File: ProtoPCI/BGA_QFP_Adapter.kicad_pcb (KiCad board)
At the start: 2 copper layers, 31 x 31 mm, 2 parts

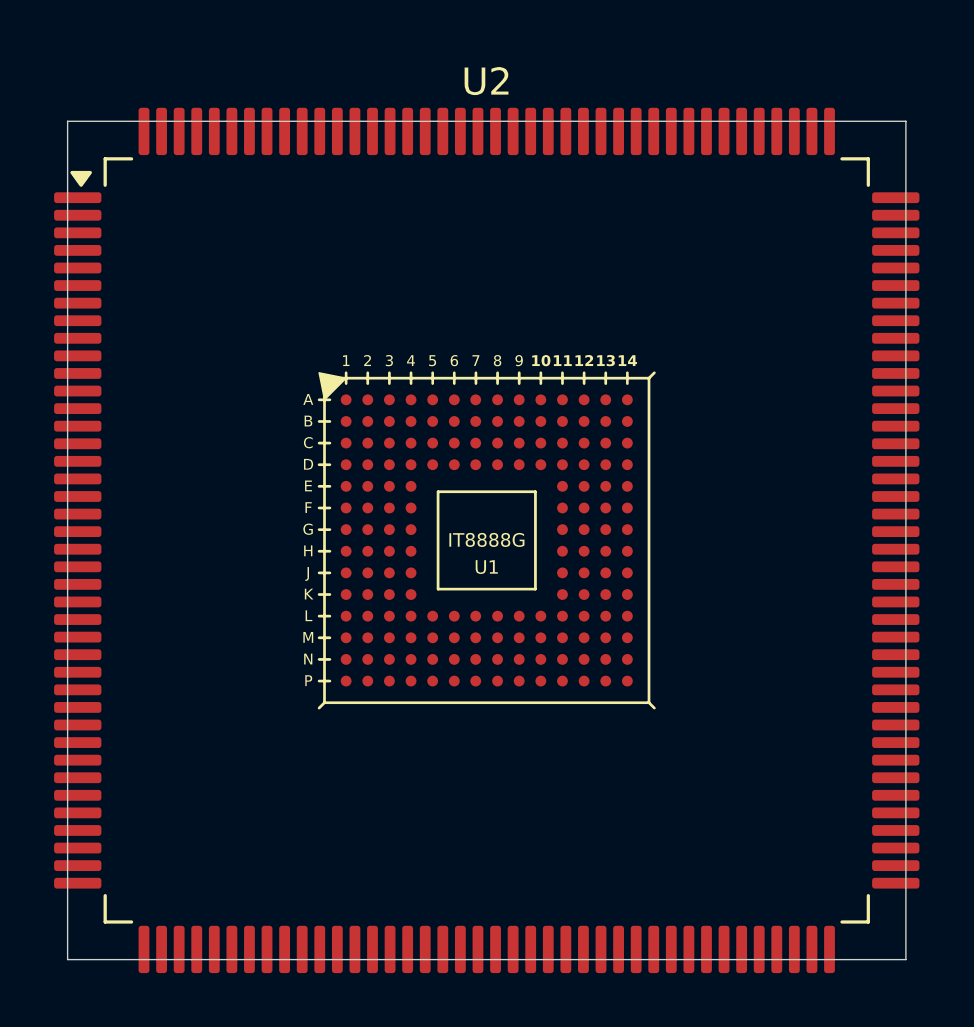
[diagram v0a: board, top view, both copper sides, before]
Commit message: Initial BGA to QFP Adapter for QFP replacement via BGA
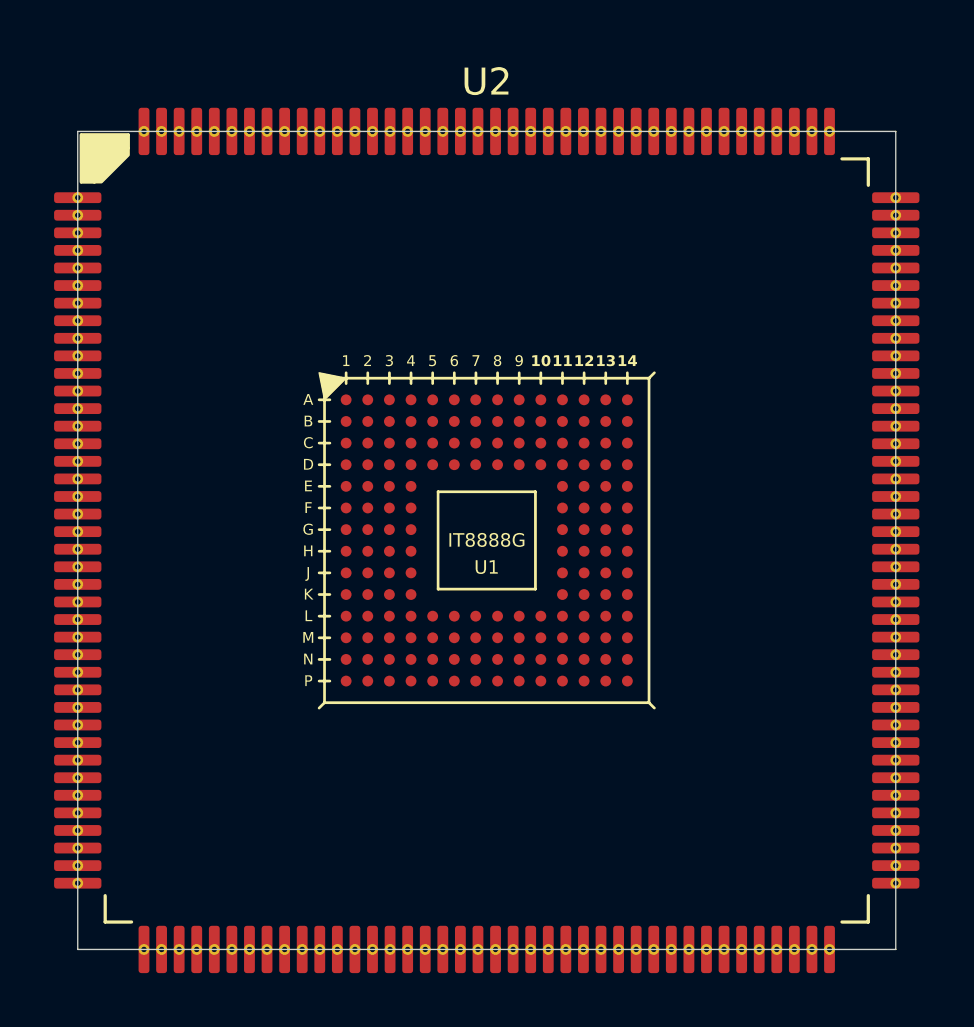
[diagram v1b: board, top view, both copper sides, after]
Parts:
- U2: footprint Package_QFP:PQFP-160_28x28mm_P0.65mm -> DFT:DFT_PQFP-160_28x28mm_P0.65mm_Adapter
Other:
- board size 31 x 31 mm -> 30.2 x 30.2 mm

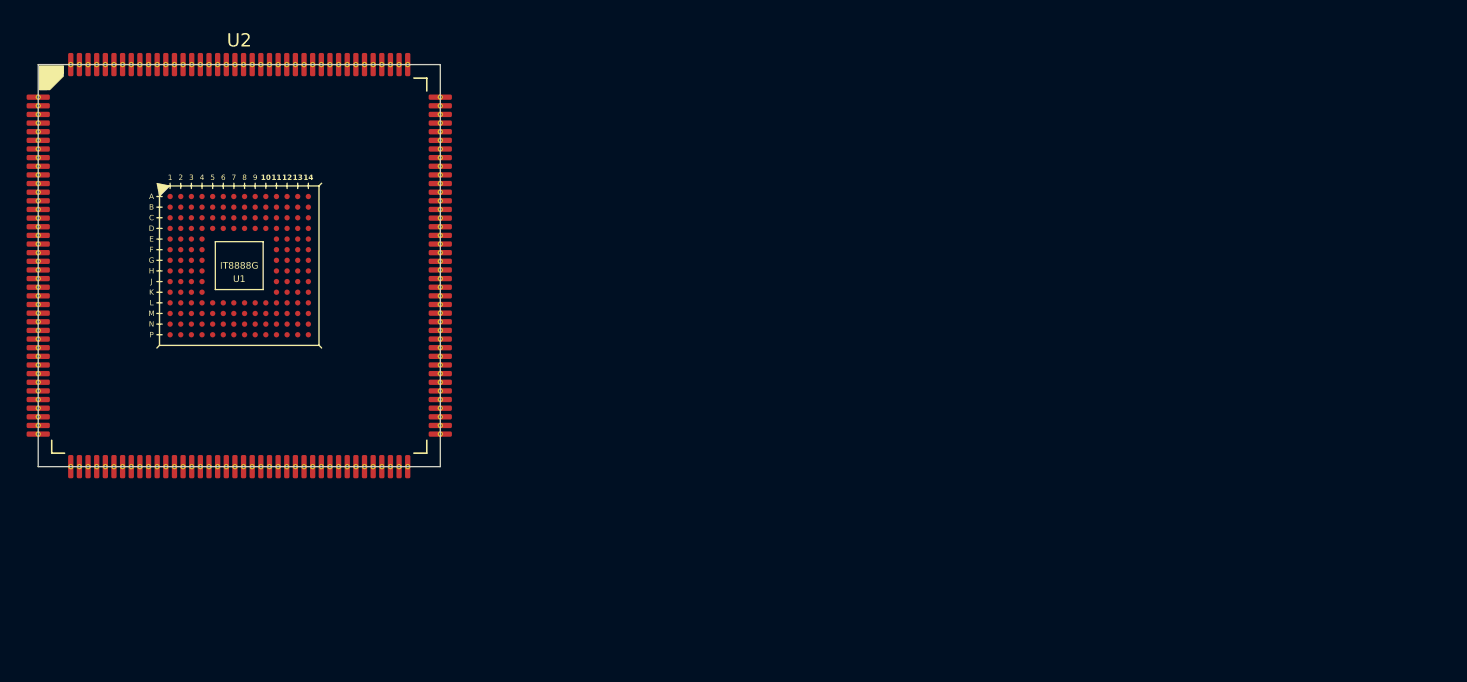
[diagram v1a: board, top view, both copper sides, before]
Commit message: BGA/QFP Adapter Setup
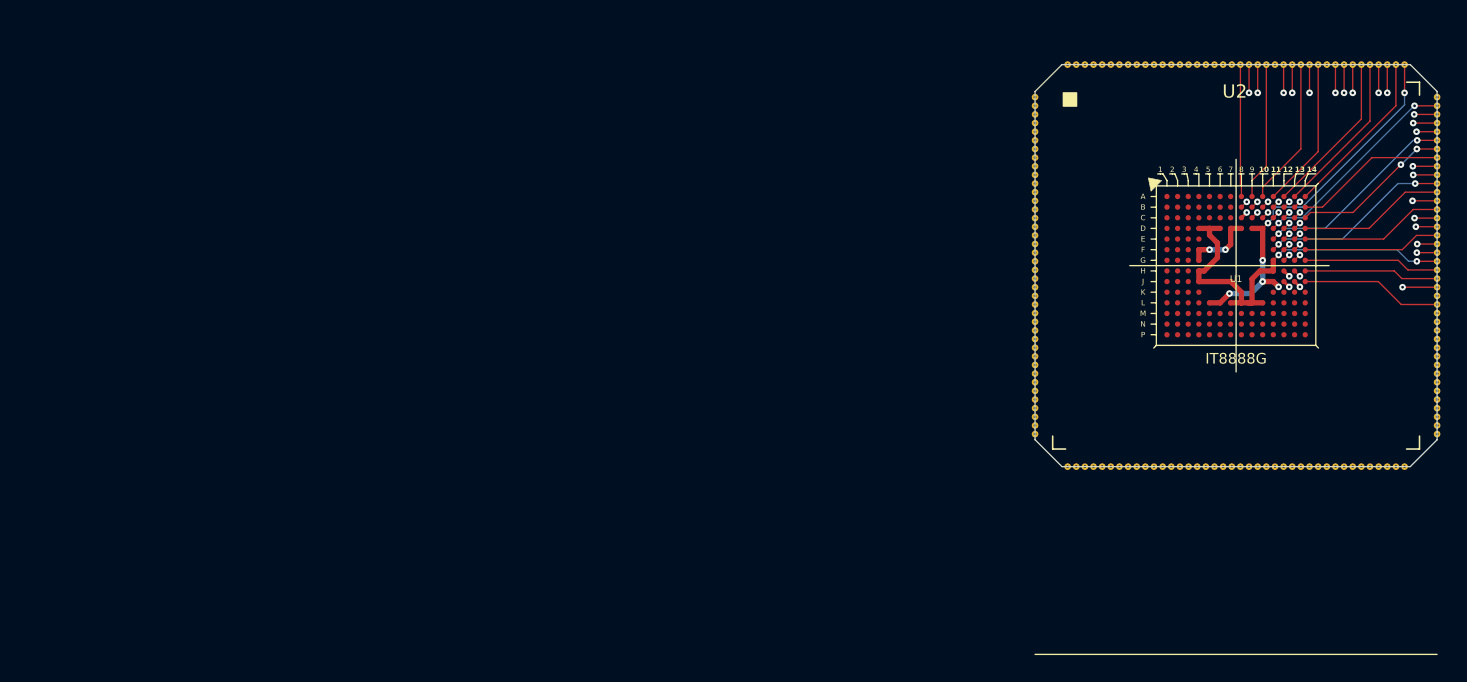
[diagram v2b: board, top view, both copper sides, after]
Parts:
- U1: footprint DFT:IT8888G -> DFT:IT8888G_QFP_Naming
- moved U1 75.0 mm to (166.6, 115.4)
- moved U2 75.0 mm to (166.6, 115.4)
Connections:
- U2 pad 1: Net-(U1-VCC3-Pad1) -> /VCC3
- U2 pad 101: Net-(U1-GND-Pad101) -> /GND
- U2 pad 120: Net-(U1-GND-Pad120) -> /GND
- U2 pad 121: Net-(U1-VCC-Pad121) -> /VCC
- U2 pad 130: Net-(U1-VCC3-Pad130) -> /VCC3
- U2 pad 136: Net-(U1-GND-Pad136) -> /GND
- U2 pad 146: Net-(U1-VCC3-Pad146) -> /VCC3
- U2 pad 148: Net-(U1-GND-Pad148) -> /GND
- U2 pad 160: Net-(U1-GND-Pad160) -> /GND
- U2 pad 18: Net-(U1-GND-Pad18) -> /GND
- U2 pad 22: Net-(U1-VCC3-Pad22) -> /VCC3
- U2 pad 28: Net-(U1-GND-Pad28) -> /GND
- U2 pad 40: Net-(U1-GND-Pad40) -> /GND
- U2 pad 41: Net-(U1-VCC-Pad41) -> /VCC
- U2 pad 52: Net-(U1-GND-Pad52) -> /GND
- U2 pad 69: Net-(U1-GND-Pad69) -> /GND
- U2 pad 80: Net-(U1-GND-Pad80) -> /GND
- U2 pad 81: Net-(U1-VCC-Pad81) -> /VCC
- U2 pad 91: Net-(U1-GND-Pad91) -> /GND
- U2 pad 93: Net-(U1-VCC-Pad93) -> /VCC
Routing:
- net /GND: track 0.00 -> 31.1 mm, vias 0 -> 2
- net /VCC: track 0.00 -> 28.6 mm, vias 0 -> 6
- net Net-(U1-LA23): track 0.00 -> 16.0 mm, vias 0 -> 2
- net Net-(U1-SA19): track 0.00 -> 15.3 mm, vias 0 -> 2
- net Net-(U1-LA22): track 0.00 -> 15.0 mm, vias 0 -> 2
- net Net-(U1-SD9): track 0.00 -> 14.6 mm, vias 0 -> 2
- net Net-(U1-LA20): track 0.00 -> 14.4 mm, vias 0 -> 2
- net Net-(U1-SD6): track 0.00 -> 14.3 mm, vias 0 -> 2
- net Net-(U1-SD14): track 0.00 -> 14.0 mm, vias 0 -> 2
- net Net-(U1-SD13): track 0.00 -> 13.9 mm, vias 0 -> 2
- net Net-(U1-SA16): track 0.00 -> 13.7 mm, vias 0 -> 2
- net Net-(U1-SD10): track 0.00 -> 13.6 mm, vias 0 -> 2
- net Net-(U1-LA21): track 0.00 -> 13.2 mm, vias 0 -> 2
- net Net-(U1-SERIRQ): track 0.00 -> 12.7 mm, vias 0 -> 2
- net Net-(U1-SD8): track 0.00 -> 12.7 mm
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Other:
- outline, holes or cut-outs redrawn
- copper layers 2 -> 4
